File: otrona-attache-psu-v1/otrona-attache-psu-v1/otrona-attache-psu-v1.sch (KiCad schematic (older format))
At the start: 17 parts, among them J1 VIDEO, J2 CPU, J3 DRIVES, J4 15V_CONV, J5 ATX-24, J6 PWR, J7 FAN

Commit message: [otrona] Update schematic, layout, part selection
so far so good... now to print it out and see
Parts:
- C1, C2, C3, C4: footprint (none) -> Capacitor_THT:CP_Radial_D10.0mm_P5.00mm
- J1: footprint (none) -> Connector_Phoenix_MSTB:PhoenixContact_MSTBVA_2,5_5-G-5,08_1x05_P5.08mm_Vertical
- J2: footprint (none) -> Connector_Phoenix_MSTB:PhoenixContact_MSTBVA_2,5_12-G-5,08_1x12_P5.08mm_Vertical
- J3: footprint (none) -> Connector_Phoenix_MSTB:PhoenixContact_MSTBVA_2,5_8-G-5,08_1x08_P5.08mm_Vertical
- J4: footprint (none) -> Connector_PinHeader_2.54mm:PinHeader_1x04_P2.54mm_Horizontal
- J5: footprint (none) -> Connector_Molex:Molex_Mini-Fit_Jr_5566-24A2_2x12_P4.20mm_Vertical
- J6, J7: footprint (none) -> Connector_PinHeader_2.54mm:PinHeader_1x02_P2.54mm_Horizontal
- L1, L2, L3, L4, L5, L6: footprint (none) -> Inductor_THT:L_Axial_L11.0mm_D4.5mm_P15.24mm_Horizontal_Fastron_MECC

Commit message: [otrona] ok fine i routed the damned board
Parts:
- added J8: AUDIO, Connector_PinHeader_2.54mm:PinHeader_1x02_P2.54mm_Horizontal, symbol Connector:Conn_01x02_Male
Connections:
- net VIDEO_HSYNC is gone; now on net DISPLAY_HSYNC: J1.5 (Pin_5)
- net SPK_AUDIO: now also J8.2 (Pin_2)
- net SPK_GND: now also J8.1 (Pin_1)
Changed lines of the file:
@@
 DISPLAY_VIDEO
 Text GLabel 9800 1600 0    50   Input ~ 0
-VIDEO_HSYNC
+DISPLAY_HSYNC
 $Comp
 L power:GND #PWR0104
@@
 	1    0    0    -1
 $EndComp
+$Comp
+L Connector:Conn_01x02_Male J8
+U 1 1 62824E1A
+P 8800 5700
+F 0 "J8" H 8772 5674 50  0000 R CNN
+F 1 "AUDIO" H 8772 5583 50  0000 R CNN
+F 2 "Connector_PinHeader_2.54mm:PinHeader_1x02_P2.54mm_Horizontal" H 8800 5700 50  0001 C CNN
+F 3 "~" H 8800 5700 50  0001 C CNN
+	1    8800 5700
+	-1   0    0    -1
+$EndComp
+Text GLabel 8600 5800 0    50   Input ~ 0
+SPK_AUDIO
+Text GLabel 8600 5700 0    50   Input ~ 0
+SPK_GND
 $EndSCHEMATC

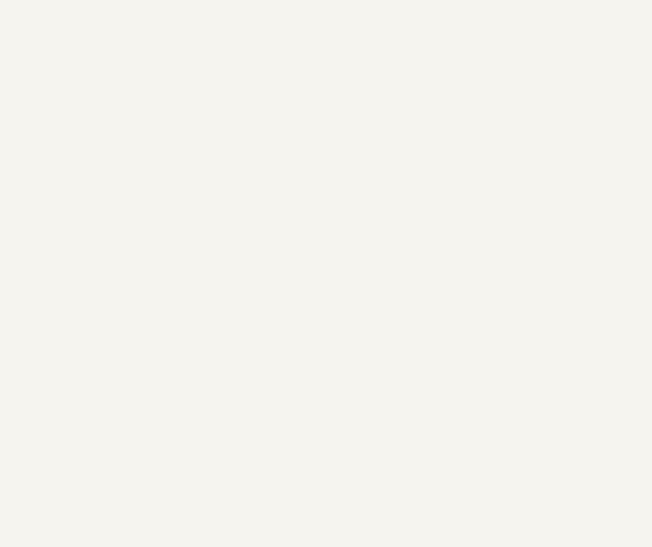
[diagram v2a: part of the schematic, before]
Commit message: Fix initial hole placings and board size, connector spacing
I still may need to tweak the top/bottom of the board clearance
but at least now this SHOULD work.

Also fix the connector spacing, I got it super bloody wrong.

I still need to fix the pad size on the ATX connector, le sigh.
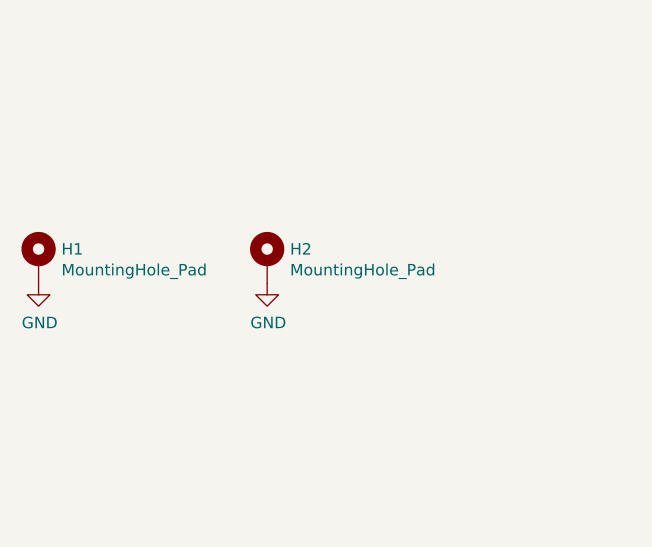
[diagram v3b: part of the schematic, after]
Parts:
- added H1, H2: MountingHole_Pad, MountingHole:MountingHole_3.5mm, symbol Mechanical:MountingHole_Pad
- J1: footprint Connector_Phoenix_MSTB:PhoenixContact_MSTBVA_2,5_5-G-5,08_1x05_P5.08mm_Vertical -> Connector_Molex:Molex_KK-396_A-41791-0005_1x05_P3.96mm_Vertical
- J2: footprint Connector_Phoenix_MSTB:PhoenixContact_MSTBVA_2,5_12-G-5,08_1x12_P5.08mm_Vertical -> Connector_Molex:Molex_KK-396_A-41791-0012_1x12_P3.96mm_Vertical
- J3: footprint Connector_Phoenix_MSTB:PhoenixContact_MSTBVA_2,5_8-G-5,08_1x08_P5.08mm_Vertical -> Connector_Molex:Molex_KK-396_A-41791-0008_1x08_P3.96mm_Vertical
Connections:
- net GND: now also H1.1, H2.1
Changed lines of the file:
@@
 F 0 "J1" H 9972 1424 50  0000 R CNN
 F 1 "VIDEO" H 9972 1333 50  0000 R CNN
-F 2 "Connector_Phoenix_MSTB:PhoenixContact_MSTBVA_2,5_5-G-5,08_1x05_P5.08mm_Vertical" H 10000 1400 50  0001 C CNN
+F 2 "Connector_Molex:Molex_KK-396_A-41791-0005_1x05_P3.96mm_Vertical" H 10000 1400 50  0001 C CNN
 F 3 "~" H 10000 1400 50  0001 C CNN
 	1    10000 1400
@@
 F 0 "J2" H 9972 2324 50  0000 R CNN
 F 1 "CPU" H 9972 2233 50  0000 R CNN
-F 2 "Connector_Phoenix_MSTB:PhoenixContact_MSTBVA_2,5_12-G-5,08_1x12_P5.08mm_Vertical" H 10000 2350 50  0001 C CNN
+F 2 "Connector_Molex:Molex_KK-396_A-41791-0012_1x12_P3.96mm_Vertical" H 10000 2350 50  0001 C CNN
 F 3 "~" H 10000 2350 50  0001 C CNN
 	1    10000 2350
@@
 F 0 "J3" H 9972 3474 50  0000 R CNN
 F 1 "DRIVES" H 9972 3383 50  0000 R CNN
-F 2 "Connector_Phoenix_MSTB:PhoenixContact_MSTBVA_2,5_8-G-5,08_1x08_P5.08mm_Vertical" H 10000 3500 50  0001 C CNN
+F 2 "Connector_Molex:Molex_KK-396_A-41791-0008_1x08_P3.96mm_Vertical" H 10000 3500 50  0001 C CNN
 F 3 "~" H 10000 3500 50  0001 C CNN
 	1    10000 3500
@@
 Text GLabel 8600 5700 0    50   Input ~ 0
 SPK_GND
+$Comp
+L Mechanical:MountingHole_Pad H1
+U 1 1 62A852AD
+P 1550 4900
+F 0 "H1" H 1650 4949 50  0000 L CNN
+F 1 "MountingHole_Pad" H 1650 4858 50  0000 L CNN
+F 2 "MountingHole:MountingHole_3.5mm" H 1550 4900 50  0001 C CNN
+F 3 "~" H 1550 4900 50  0001 C CNN
+	1    1550 4900
+	1    0    0    -1
+$EndComp
+$Comp
+L power:GND #PWR0127
+U 1 1 62A86485
+P 1550 5000
+F 0 "#PWR0127" H 1550 4750 50  0001 C CNN
+F 1 "GND" H 1555 4827 50  0000 C CNN
+F 2 "" H 1550 5000 50  0001 C CNN
+F 3 "" H 1550 5000 50  0001 C CNN
+	1    1550 5000
+	1    0    0    -1
+$EndComp
+$Comp
+L Mechanical:MountingHole_Pad H2
+U 1 1 62A86803
+P 2550 4900
+F 0 "H2" H 2650 4949 50  0000 L CNN
+F 1 "MountingHole_Pad" H 2650 4858 50  0000 L CNN
+F 2 "MountingHole:MountingHole_3.5mm" H 2550 4900 50  0001 C CNN
+F 3 "~" H 2550 4900 50  0001 C CNN
+	1    2550 4900
+	1    0    0    -1
+$EndComp
+$Comp
+L power:GND #PWR0128
+U 1 1 62A86809
+P 2550 5000
+F 0 "#PWR0128" H 2550 4750 50  0001 C CNN
+F 1 "GND" H 2555 4827 50  0000 C CNN
+F 2 "" H 2550 5000 50  0001 C CNN
+F 3 "" H 2550 5000 50  0001 C CNN
+	1    2550 5000
+	1    0    0    -1
+$EndComp
 $EndSCHEMATC

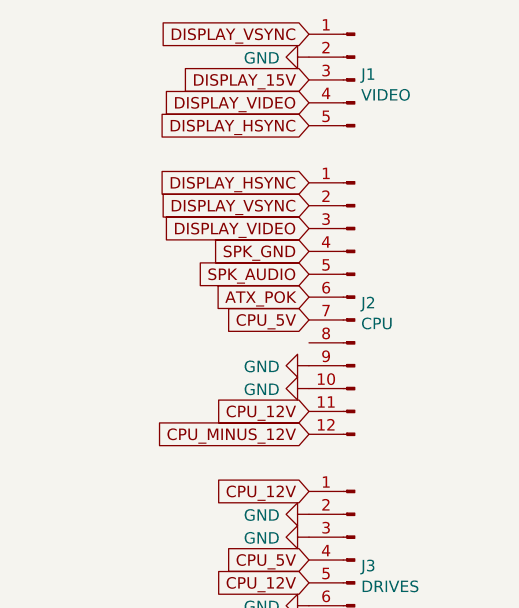
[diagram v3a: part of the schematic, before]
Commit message: start re-laying things out, after my previous board just didn't fit right.
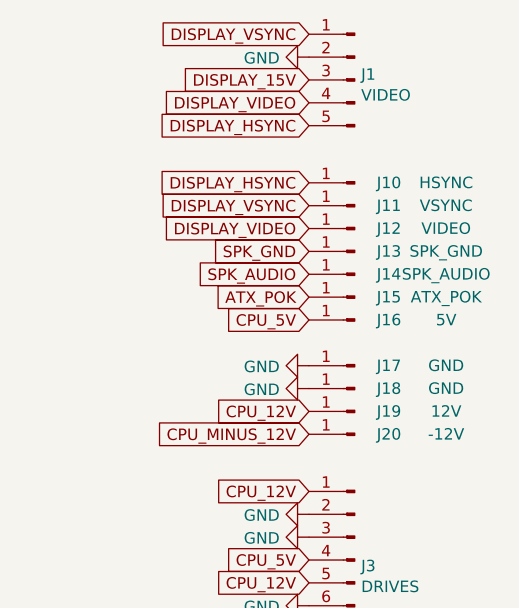
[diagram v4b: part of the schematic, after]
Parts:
- removed J2: CPU, Connector_Molex:Molex_KK-396_A-41791-0012_1x12_P3.96mm_Vertical, symbol Connector:Conn_01x12_Male
- added J10: HSYNC, Connector_Wire:SolderWire-0.75sqmm_1x01_D1.25mm_OD3.5mm, symbol Connector:Conn_01x01_Male
- added J11: VSYNC, Connector_Wire:SolderWire-0.75sqmm_1x01_D1.25mm_OD3.5mm, symbol Connector:Conn_01x01_Male
- added J12: VIDEO, Connector_Wire:SolderWire-0.75sqmm_1x01_D1.25mm_OD3.5mm, symbol Connector:Conn_01x01_Male
- added J13: SPK_GND, Connector_Wire:SolderWire-0.75sqmm_1x01_D1.25mm_OD3.5mm, symbol Connector:Conn_01x01_Male
- added J14: SPK_AUDIO, Connector_Wire:SolderWire-0.75sqmm_1x01_D1.25mm_OD3.5mm, symbol Connector:Conn_01x01_Male
- added J15: ATX_POK, Connector_Wire:SolderWire-0.75sqmm_1x01_D1.25mm_OD3.5mm, symbol Connector:Conn_01x01_Male
- added J16: 5V, Connector_Wire:SolderWire-0.75sqmm_1x01_D1.25mm_OD3.5mm, symbol Connector:Conn_01x01_Male
- added J17, J18: GND, Connector_Wire:SolderWire-0.75sqmm_1x01_D1.25mm_OD3.5mm, symbol Connector:Conn_01x01_Male
- added J19: 12V, Connector_Wire:SolderWire-0.75sqmm_1x01_D1.25mm_OD3.5mm, symbol Connector:Conn_01x01_Male
- added J20: -12V, Connector_Wire:SolderWire-0.75sqmm_1x01_D1.25mm_OD3.5mm, symbol Connector:Conn_01x01_Male
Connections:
- net ATX_POK: now also J15.1 (Pin_1)
- net CPU_12V: now also J19.1 (Pin_1)
- net CPU_5V: now also J16.1 (Pin_1)
- net CPU_MINUS_12V: now also J20.1 (Pin_1)
- net DISPLAY_HSYNC: now also J10.1 (Pin_1)
- net DISPLAY_VIDEO: now also J12.1 (Pin_1)
- net DISPLAY_VSYNC: now also J11.1 (Pin_1)
- net GND: now also J17.1 (Pin_1), J18.1 (Pin_1)
- net SPK_AUDIO: now also J14.1 (Pin_1)
- net SPK_GND: now also J13.1 (Pin_1)
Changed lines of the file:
@@
-$EndComp
-$Comp
-L Connector:Conn_01x12_Male J2
-U 1 1 61D2A493
-P 10000 2350
-F 0 "J2" H 9972 2324 50  0000 R CNN
-F 1 "CPU" H 9972 2233 50  0000 R CNN
-F 2 "Connector_Molex:Molex_KK-396_A-41791-0012_1x12_P3.96mm_Vertical" H 10000 2350 50  0001 C CNN
-F 3 "~" H 10000 2350 50  0001 C CNN
-	1    10000 2350
-	-1   0    0    -1
 $EndComp
 $Comp
@@
 	1    0    0    -1
 $EndComp
+$Comp
+L Connector:Conn_01x01_Male J10
+U 1 1 6402FF03
+P 10000 1850
+F 0 "J10" H 9850 1850 50  0000 C CNN
+F 1 "HSYNC" H 9600 1850 50  0000 C CNN
+F 2 "Connector_Wire:SolderWire-0.75sqmm_1x01_D1.25mm_OD3.5mm" H 10000 1850 50  0001 C CNN
+F 3 "~" H 10000 1850 50  0001 C CNN
+	1    10000 1850
+	-1   0    0    -1
+$EndComp
+$Comp
+L Connector:Conn_01x01_Male J11
+U 1 1 64064B92
+P 10000 1950
+F 0 "J11" H 9850 1950 50  0000 C CNN
+F 1 "VSYNC" H 9600 1950 50  0000 C CNN
+F 2 "Connector_Wire:SolderWire-0.75sqmm_1x01_D1.25mm_OD3.5mm" H 10000 1950 50  0001 C CNN
+F 3 "~" H 10000 1950 50  0001 C CNN
+	1    10000 1950
+	-1   0    0    -1
+$EndComp
+$Comp
+L Connector:Conn_01x01_Male J12
+U 1 1 640659B4
+P 10000 2050
+F 0 "J12" H 9850 2050 50  0000 C CNN
+F 1 "VIDEO" H 9600 2050 50  0000 C CNN
+F 2 "Connector_Wire:SolderWire-0.75sqmm_1x01_D1.25mm_OD3.5mm" H 10000 2050 50  0001 C CNN
+F 3 "~" H 10000 2050 50  0001 C CNN
+	1    10000 2050
+	-1   0    0    -1
+$EndComp
+$Comp
+L Connector:Conn_01x01_Male J13
+U 1 1 6406620A
+P 10000 2150
+F 0 "J13" H 9850 2150 50  0000 C CNN
+F 1 "SPK_GND" H 9600 2150 50  0000 C CNN
+F 2 "Connector_Wire:SolderWire-0.75sqmm_1x01_D1.25mm_OD3.5mm" H 10000 2150 50  0001 C CNN
+F 3 "~" H 10000 2150 50  0001 C CNN
+	1    10000 2150
+	-1   0    0    -1
+$EndComp
+$Comp
+L Connector:Conn_01x01_Male J14
+U 1 1 640668EC
+P 10000 2250
+F 0 "J14" H 9850 2250 50  0000 C CNN
+F 1 "SPK_AUDIO" H 9600 2250 50  0000 C CNN
+F 2 "Connector_Wire:SolderWire-0.75sqmm_1x01_D1.25mm_OD3.5mm" H 10000 2250 50  0001 C CNN
+F 3 "~" H 10000 2250 50  0001 C CNN
+	1    10000 2250
+	-1   0    0    -1
+$EndComp
+$Comp
+L Connector:Conn_01x01_Male J15
+U 1 1 64066F93
+P 10000 2350
+F 0 "J15" H 9850 2350 50  0000 C CNN
+F 1 "ATX_POK" H 9600 2350 50  0000 C CNN
+F 2 "Connector_Wire:SolderWire-0.75sqmm_1x01_D1.25mm_OD3.5mm" H 10000 2350 50  0001 C CNN
+F 3 "~" H 10000 2350 50  0001 C CNN
+	1    10000 2350
+	-1   0    0    -1
+$EndComp
+$Comp
+L Connector:Conn_01x01_Male J16
+U 1 1 64067382
+P 10000 2450
+F 0 "J16" H 9850 2450 50  0000 C CNN
+F 1 "5V" H 9600 2450 50  0000 C CNN
+F 2 "Connector_Wire:SolderWire-0.75sqmm_1x01_D1.25mm_OD3.5mm" H 10000 2450 50  0001 C CNN
+F 3 "~" H 10000 2450 50  0001 C CNN
+	1    10000 2450
+	-1   0    0    -1
+$EndComp
+$Comp
+L Connector:Conn_01x01_Male J17
+U 1 1 64067B69
+P 10000 2650
+F 0 "J17" H 9850 2650 50  0000 C CNN
+F 1 "GND" H 9600 2650 50  0000 C CNN
+F 2 "Connector_Wire:SolderWire-0.75sqmm_1x01_D1.25mm_OD3.5mm" H 10000 2650 50  0001 C CNN
+F 3 "~" H 10000 2650 50  0001 C CNN
+	1    10000 2650
+	-1   0    0    -1
+$EndComp
+$Comp
+L Connector:Conn_01x01_Male J18
+U 1 1 640681B5
+P 10000 2750
+F 0 "J18" H 9850 2750 50  0000 C CNN
+F 1 "GND" H 9600 2750 50  0000 C CNN
+F 2 "Connector_Wire:SolderWire-0.75sqmm_1x01_D1.25mm_OD3.5mm" H 10000 2750 50  0001 C CNN
+F 3 "~" H 10000 2750 50  0001 C CNN
+	1    10000 2750
+	-1   0    0    -1
+$EndComp
+$Comp
+L Connector:Conn_01x01_Male J19
+U 1 1 640687CA
+P 10000 2850
+F 0 "J19" H 9850 2850 50  0000 C CNN
+F 1 "12V" H 9600 2850 50  0000 C CNN
+F 2 "Connector_Wire:SolderWire-0.75sqmm_1x01_D1.25mm_OD3.5mm" H 10000 2850 50  0001 C CNN
+F 3 "~" H 10000 2850 50  0001 C CNN
+	1    10000 2850
+	-1   0    0    -1
+$EndComp
+$Comp
+L Connector:Conn_01x01_Male J20
+U 1 1 64068AC4
+P 10000 2950
+F 0 "J20" H 9850 2950 50  0000 C CNN
+F 1 "-12V" H 9600 2950 50  0000 C CNN
+F 2 "Connector_Wire:SolderWire-0.75sqmm_1x01_D1.25mm_OD3.5mm" H 10000 2950 50  0001 C CNN
+F 3 "~" H 10000 2950 50  0001 C CNN
+	1    10000 2950
+	-1   0    0    -1
+$EndComp
 $EndSCHEMATC
